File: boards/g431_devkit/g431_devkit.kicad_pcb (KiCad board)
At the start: 2 copper layers, 41.8 x 24.2 mm, 18 parts, among them J1 usb_c_16p, J2 samtec_ftsh_107_01_l_dv_k, U1 ht7333, U2 VAL**

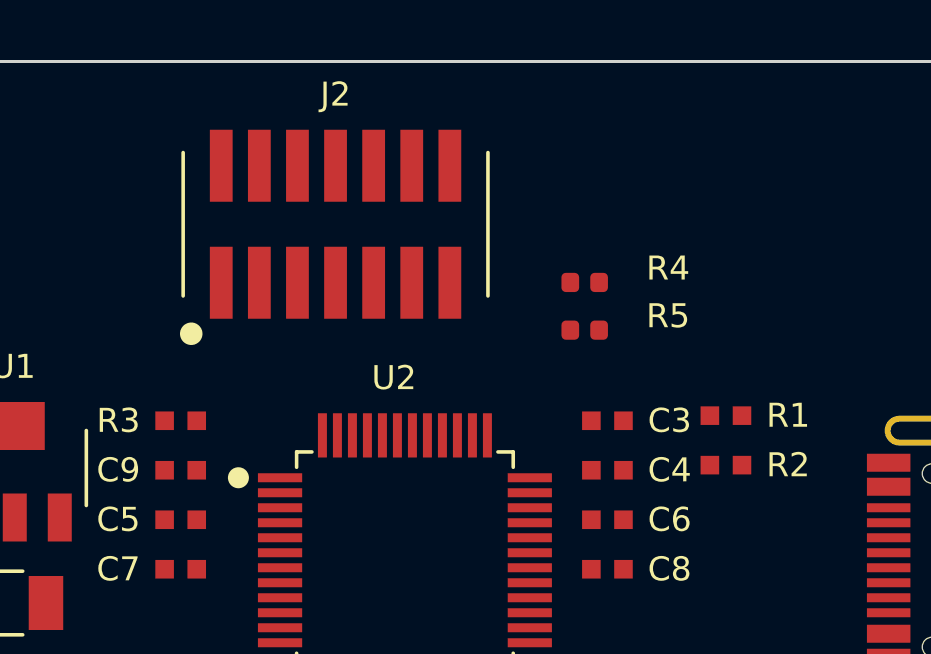
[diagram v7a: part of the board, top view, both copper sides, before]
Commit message: P12: 신호 패드가 메인 IC를 향하게 회전 (J2 180도 등)
- 부품마다 0/90/180/270 중 신호 패드 무게중심이 IC 방향과 가장 일치하는
  각 선택 — J2(STDC14) 180도(신호열 4/6/8/12/14가 MCU쪽), I2C 저항 90도.
- 가장자리 부품은 삽입구 방향(P6) 우선이라 제외. DRC 0 유지.

Co-Authored-By: Claude Fable 5 <noreply@anthropic.com>
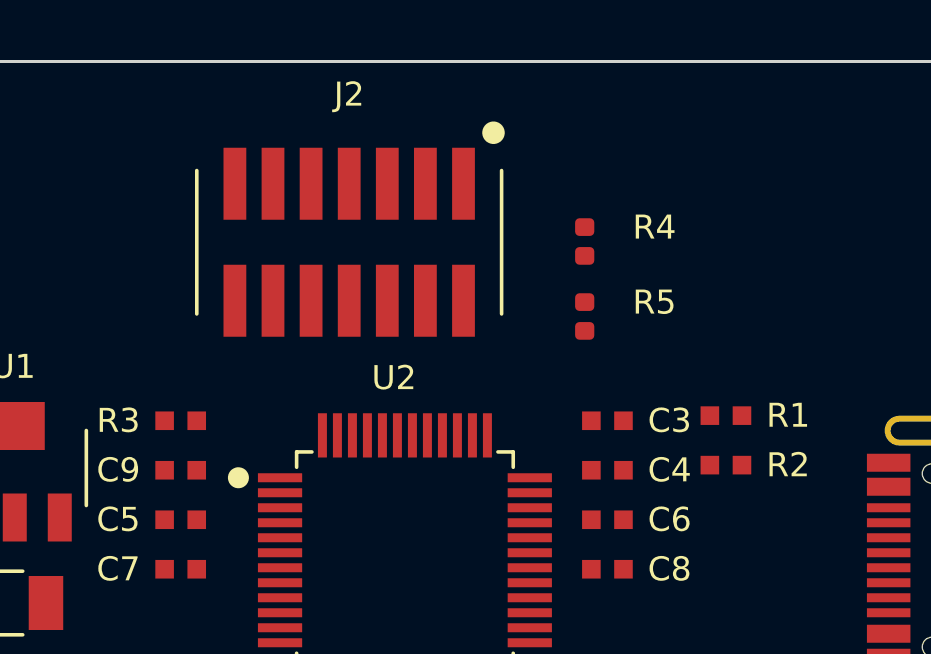
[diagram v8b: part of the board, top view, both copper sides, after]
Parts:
- moved R4 1.37 mm to (151.3, 98.9), turned to 90 degrees
- moved J2 0.75 mm to (143.4, 98.9), turned to 180 degrees
- moved R5 0.46 mm to (151.3, 101.4), turned to 90 degrees
- turned R1 to 180 degrees
- turned R2 to 180 degrees
